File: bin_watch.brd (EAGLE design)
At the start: 39.2 x 30.1 mm, 107 parts, among them IC1 MEGA48/88/168-MU, J1 USB3100-XX-X_REVB, Q1 32.768kHz, T1 2N7002BKV, T2 2N7002BKV, T3 2N7002BKV, T4 2N7002BKV, T5 PMDT670UPE, T6 PMDT670UPE, T7 PMDT670UPE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

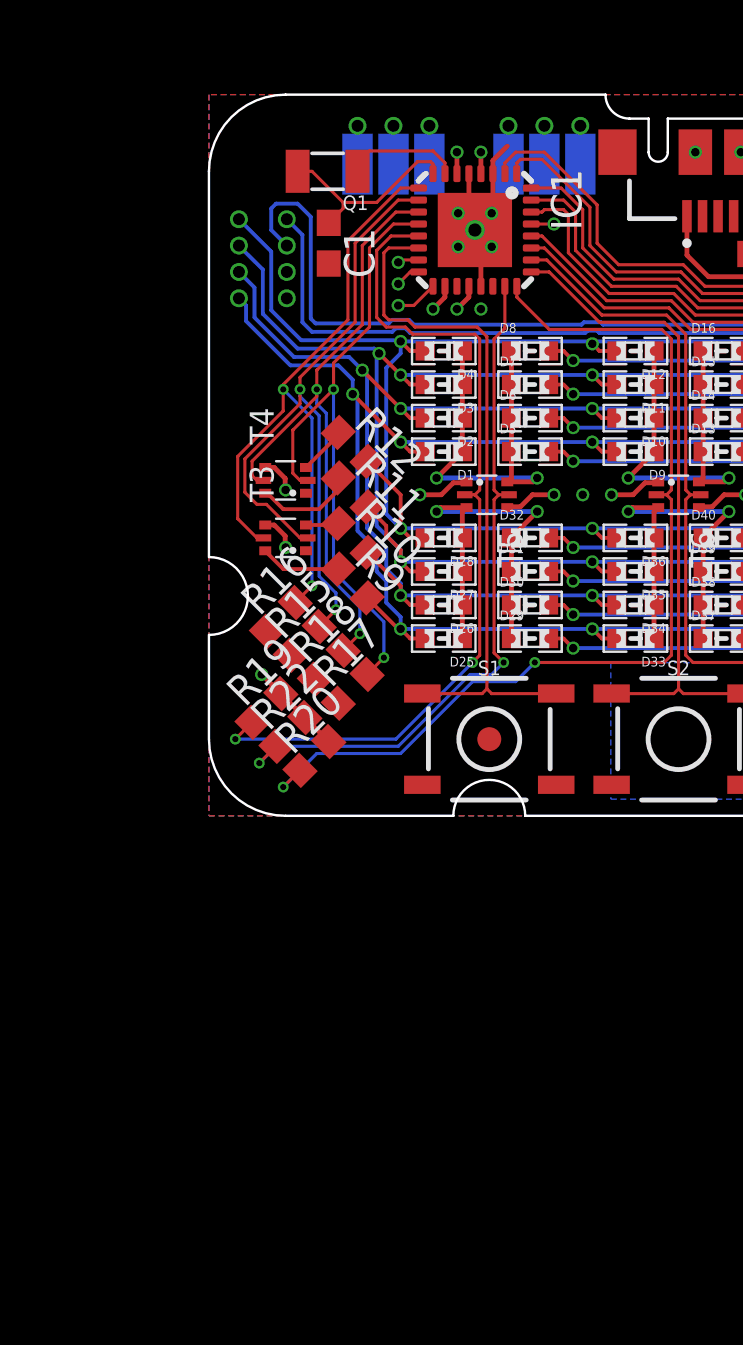
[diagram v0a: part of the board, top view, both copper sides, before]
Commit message: Removed QFN32, placed QFN28
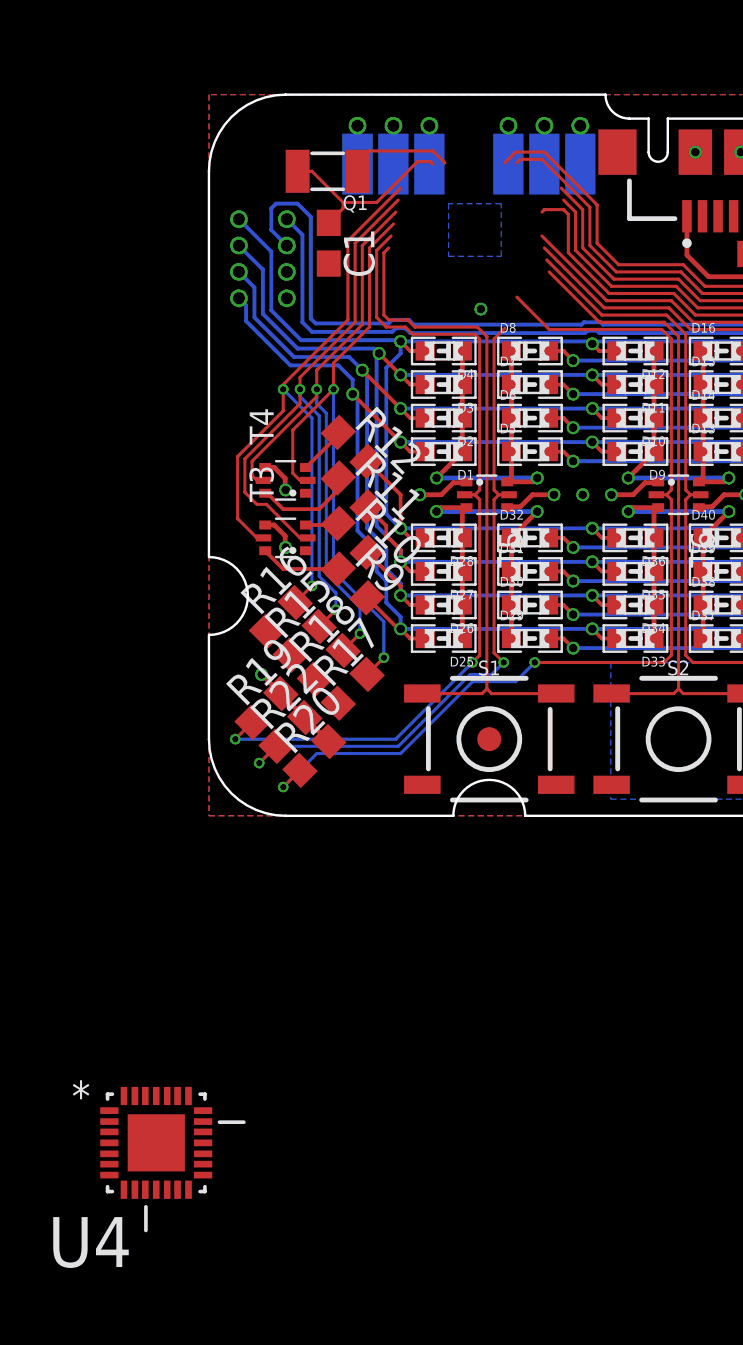
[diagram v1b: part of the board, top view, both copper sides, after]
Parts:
- removed IC1: MEGA48/88/168-MU, avr-5:MLF32
- added U4: ATMEGA48PA-MMH, Atmel_By_element14_Batch_1-00:QFN45P400X400X100-29N
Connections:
- removed net ADC6: IC1.19
- removed net ADC7: IC1.22
- removed net MISO: IC1.16
- removed net MOSI: IC1.15
- removed net RST: IC1.29
- removed net SCK: IC1.17
- new net N$10: U4.23
- new net N$11: U4.24
- new net N$12: U4.10
- new net N$13: U4.11
- new net N$14: U4.12
- new net N$15: U4.26
- new net N$2: U4.13
- new net N$21: U4.8
- new net N$22: U4.9
- new net N$3: U4.25
- new net N$4: U4.14
- new net N$5: U4.15
- net BTN1: no longer IC1.14
- net BTN2: no longer IC1.25
- net BTN3: no longer IC1.28
- net GND: now also U4.18, U4.29, U4.4; no longer IC1.21, IC1.3, IC1.5
- net G_BLOCK0: now also U4.7; no longer IC1.13
- net G_BLOCK1: no longer IC1.24
- net G_BLOCK2: no longer IC1.27
- net G_BLOCK3: no longer IC1.23
- net G_BLOCK4: no longer IC1.26
- net G_BLOCK5: no longer IC1.30
- net G_LIGHT0: now also U4.21; no longer IC1.1
- net G_LIGHT1: now also U4.22; no longer IC1.2
- net G_LIGHT2: now also U4.19; no longer IC1.31
- net G_LIGHT3: now also U4.20; no longer IC1.32
- net G_LIGHT4: now also U4.28; no longer IC1.10
- net G_LIGHT5: now also U4.27; no longer IC1.9
- net G_LIGHT6: now also U4.2; no longer IC1.12
- net G_LIGHT7: now also U4.1; no longer IC1.11
- net VCC: now also U4.16, U4.17, U4.3; no longer IC1.18, IC1.20, IC1.4, IC1.6
- net XTAL_N: now also U4.6; no longer IC1.8
- net XTAL_P: now also U4.5; no longer IC1.7
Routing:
- net GND: track 31.4 -> 8.31 mm, vias 19 -> 14
- net VCC: track 32.3 -> 28.1 mm, vias 14 -> 10
- net SCK: track 1.78 -> 0.00 mm, vias 1 -> 0
- net G_BLOCK3: track 29.6 -> 27.8 mm
- net G_LIGHT2: track 38.8 -> 37.5 mm
- net G_LIGHT3: track 45.3 -> 44.0 mm
- net BTN1: track 29.3 -> 28.0 mm
- net G_BLOCK0: track 35.9 -> 34.8 mm
- net MISO: track 1.06 -> 0.00 mm, vias 1 -> 0
- net G_LIGHT6: track 27.0 -> 25.9 mm
- net G_LIGHT7: track 26.9 -> 26.0 mm
- net RST: track 0.95 -> 0.00 mm, vias 1 -> 0
- net MOSI: track 0.89 -> 0.00 mm, vias 1 -> 0
- net G_LIGHT4: track 29.9 -> 29.1 mm
- net G_LIGHT5: track 28.5 -> 27.7 mm
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
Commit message: New chip wired to IO
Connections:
- removed net N$12: U4.10
- removed net N$13: U4.11
- removed net N$14: U4.12
- removed net N$2: U4.13
- removed net N$21: U4.8
- removed net N$22: U4.9
- removed net N$4: U4.14
- removed net N$5: U4.15
- net BTN1: now also U4.8
- net BTN2: now also U4.11
- net BTN3: now also U4.14
- net G_BLOCK1: now also U4.10
- net G_BLOCK2: now also U4.13
- net G_BLOCK3: now also U4.9
- net G_BLOCK4: now also U4.12
- net G_BLOCK5: now also U4.15
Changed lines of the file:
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@@
 <wire x1="8.6" y1="20.4" x2="11.2" y2="20.4" width="0.13" layer="1"/>
 <wire x1="11.2" y1="20.4" x2="11.6" y2="20" width="0.13" layer="1"/>
+<contactref element="U4" pad="8"/>
+<wire x1="8.911" y1="5.1" x2="-3.5462" y2="-15.6058" width="0" layer="19" extent="1-1"/>
 </signal>
 <signal name="BTN2" class="4">
@@
 <wire x1="16.3" y1="20.6" x2="19" y2="20.6" width="0.13" layer="1"/>
 <wire x1="19" y1="20.6" x2="19.6" y2="20" width="0.13" layer="1"/>
+<contactref element="U4" pad="11"/>
+<wire x1="-2.2" y1="-15.6058" x2="16.806" y2="5.105" width="0" layer="19" extent="1-1"/>
 </signal>
 <signal name="BTN3" class="4">
@@
 <wire x1="19.3" y1="21.5" x2="20.2" y2="20.6" width="0.13" layer="1"/>
 <wire x1="20.2" y1="20.6" x2="27" y2="20.6" width="0.13" layer="1"/>
+<contactref element="U4" pad="14"/>
+<wire x1="-0.8538" y1="-15.6058" x2="24.706" y2="5.105" width="0" layer="19" extent="1-1"/>
 </signal>
 <signal name="VCC" class="1">
@@
 <wire x1="11" y1="5.6" x2="12.8" y2="5.6" width="0.13" layer="16"/>
 <wire x1="12.8" y1="5.6" x2="13.6" y2="6.4" width="0.13" layer="16"/>
+<contactref element="U4" pad="10"/>
+<wire x1="3.1" y1="1.2" x2="-2.6572" y2="-15.6058" width="0" layer="19" extent="1-1"/>
 </signal>
 <signal name="G_BLOCK2" class="4">
@@
 <wire x1="27.3" y1="6.8" x2="26.9" y2="6.4" width="0.13" layer="1"/>
 <via x="26.9" y="6.4" extent="1-16" drill="0.254"/>
+<contactref element="U4" pad="13"/>
+<wire x1="-1.311" y1="-15.6058" x2="26.9" y2="6.4" width="0" layer="19" extent="1-16"/>
 </signal>
 <signal name="G_BLOCK3" class="4">
@@
 <wire x1="10.9" y1="5.9" x2="11.8" y2="5.9" width="0.13" layer="16"/>
 <wire x1="11.8" y1="5.9" x2="12.3" y2="6.4" width="0.13" layer="16"/>
+<contactref element="U4" pad="9"/>
+<wire x1="2.1" y1="2.2" x2="-3.089" y2="-15.6058" width="0" layer="19" extent="1-1"/>
 </signal>
 <signal name="G_BLOCK4" class="4">
@@
 <wire x1="31.2" y1="2.6" x2="34.7" y2="2.6" width="0.13" layer="16"/>
 <wire x1="34.7" y1="2.6" x2="36.1" y2="1.2" width="0.13" layer="16"/>
+<contactref element="U4" pad="12"/>
+<wire x1="-1.7428" y1="-15.6058" x2="20.2" y2="6.4" width="0" layer="19" extent="1-1"/>
 </signal>
 <signal name="G_BLOCK5" class="4">
@@
 <wire x1="28.2" y1="6.4" x2="31.4" y2="3.2" width="0.13" layer="16"/>
 <wire x1="31.4" y1="3.2" x2="38.1" y2="3.2" width="0.13" layer="16"/>
+<contactref element="U4" pad="15"/>
+<wire x1="-0.2442" y1="-14.9962" x2="27.9" y2="6.7" width="0" layer="19" extent="1-1"/>
 </signal>
 <signal name="G_LIGHT0" class="4">
@@
 <contactref element="U4" pad="25"/>
 </signal>
-<signal name="N$2">
-<contactref element="U4" pad="13"/>
-</signal>
-<signal name="N$4">
-<contactref element="U4" pad="14"/>
-</signal>
-<signal name="N$5">
-<contactref element="U4" pad="15"/>
-</signal>
 <signal name="N$10">
 <contactref element="U4" pad="23"/>
@@
 <contactref element="U4" pad="24"/>
 </signal>
-<signal name="N$12">
-<contactref element="U4" pad="10"/>
-</signal>
-<signal name="N$13">
-<contactref element="U4" pad="11"/>
-</signal>
-<signal name="N$14">
-<contactref element="U4" pad="12"/>
-</signal>
 <signal name="N$15">
 <contactref element="U4" pad="26"/>
 </signal>
-<signal name="N$21">
-<contactref element="U4" pad="8"/>
-</signal>
-<signal name="N$22">
-<contactref element="U4" pad="9"/>
-</signal>
 </signals>

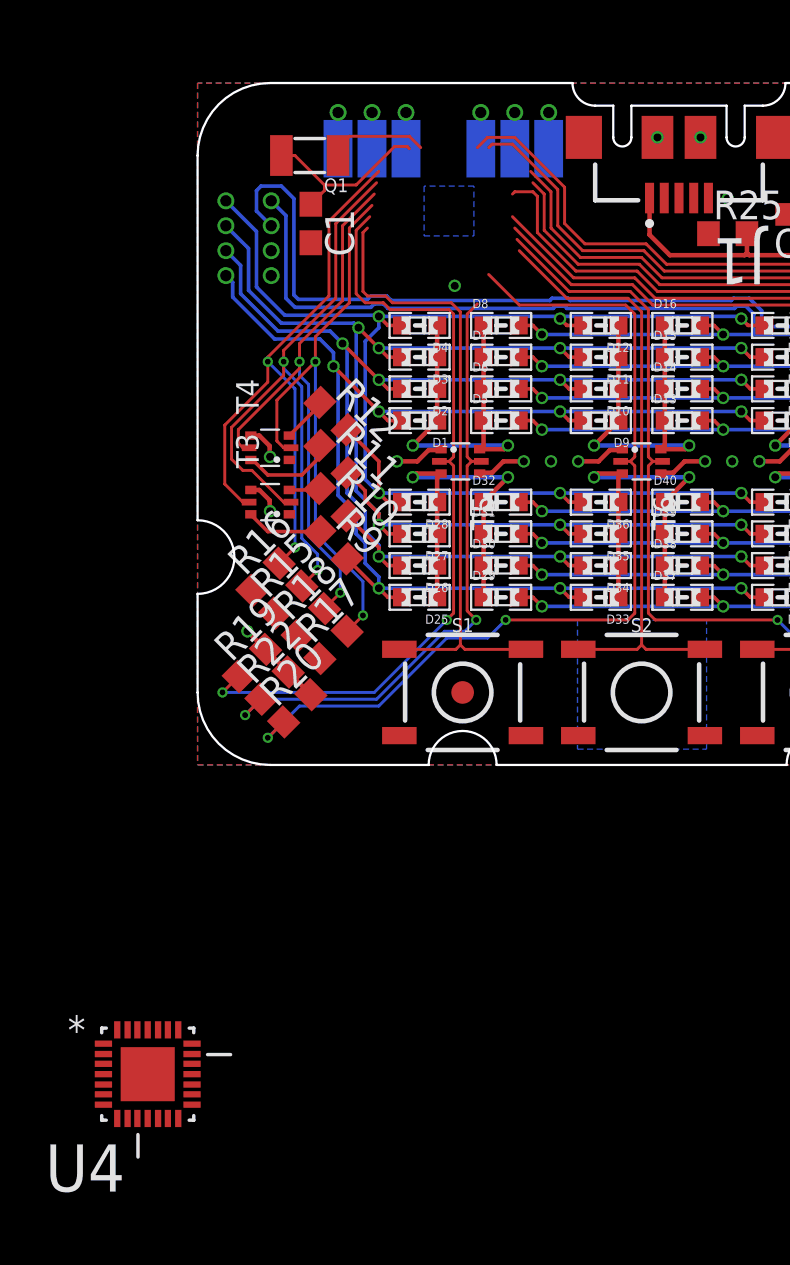
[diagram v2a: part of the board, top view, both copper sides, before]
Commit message: Routing UC to IO
WIP
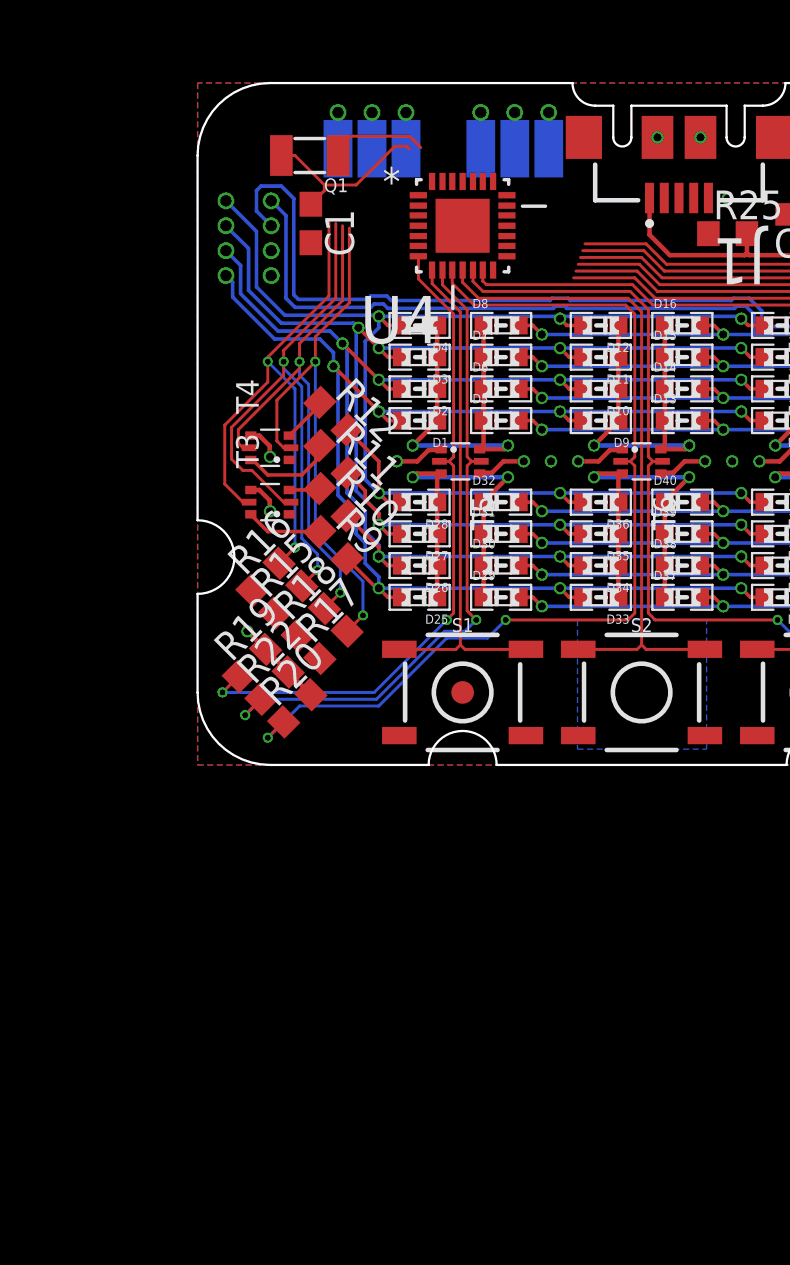
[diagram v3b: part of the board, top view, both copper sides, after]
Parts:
- moved U4 39.9 mm to (11.7, 23.8)
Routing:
- net G_LIGHT1: track 55.6 -> 47.8 mm
- net G_LIGHT0: track 48.7 -> 41.6 mm
- net G_BLOCK5: track 43.8 -> 38.5 mm
- net BTN1: track 28.0 -> 22.8 mm
- net G_BLOCK0: track 34.8 -> 29.6 mm
- net G_LIGHT3: track 44.0 -> 39.3 mm
- net G_LIGHT2: track 37.5 -> 33.0 mm
- net BTN3: track 35.9 -> 32.1 mm
- net G_LIGHT5: track 27.7 -> 24.6 mm
- net G_LIGHT4: track 29.1 -> 26.5 mm
- net BTN2: track 27.0 -> 29.4 mm
- net G_BLOCK1: track 40.4 -> 42.5 mm
- net G_LIGHT7: track 26.0 -> 24.0 mm
- net G_BLOCK3: track 27.8 -> 29.6 mm
- net G_BLOCK4: track 40.5 -> 42.2 mm
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- removed copper zone on layer 16, net GND

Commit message: More routing
WIP
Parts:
- moved Q1 5.85 mm to (8.15, 22.0), turned to 270 degrees
- moved C1 3.09 mm to (6.50, 21.2), turned to 90 degrees
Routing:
- net XTAL_N: track 8.03 -> 0.00 mm
- net G_LIGHT5: track 24.6 -> 31.1 mm
- net G_LIGHT1: track 47.8 -> 53.0 mm
- net G_LIGHT4: track 26.5 -> 31.6 mm
- net XTAL_P: track 4.41 -> 0.00 mm
- net G_LIGHT0: track 41.6 -> 45.9 mm
- net G_LIGHT3: track 39.3 -> 43.5 mm
- net G_LIGHT2: track 33.0 -> 37.1 mm
- net G_LIGHT7: track 24.0 -> 28.0 mm
- net BTN3: track 32.1 -> 35.8 mm
- net G_LIGHT6: track 24.5 -> 28.1 mm
- net G_BLOCK5: track 38.5 -> 41.8 mm
- net VCC: track 28.1 -> 29.5 mm, vias 10 -> 11

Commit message: Routed IO
TODO: ISP
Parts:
- moved C5 20.1 mm to (16.4, 22.6), turned to 0 degrees
- moved C1 0.78 mm to (6.00, 20.6)
- moved Q1 0.50 mm to (7.65, 22.0)
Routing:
- net XTAL_N: track 0.00 -> 5.79 mm
- net XTAL_P: track 0.00 -> 3.78 mm
- net G_LIGHT5: track 31.1 -> 32.0 mm
- net VCC: track 29.5 -> 28.6 mm, vias 11 -> 12
- net G_LIGHT4: track 31.6 -> 32.4 mm
- net G_LIGHT7: track 28.0 -> 28.8 mm
- net G_LIGHT6: track 28.1 -> 28.9 mm
- net GND: vias 13 -> 16
